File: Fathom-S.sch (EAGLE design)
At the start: 98 parts, among them IC1 LMH6643, IC2 LMH6643, IC3 ST490AB, IC4 ST490AB, IC5 FT230XS, Q1 BC817-40W, U1 MC7812, U2 MC7805, U5 MC7805, X2 USBSMD

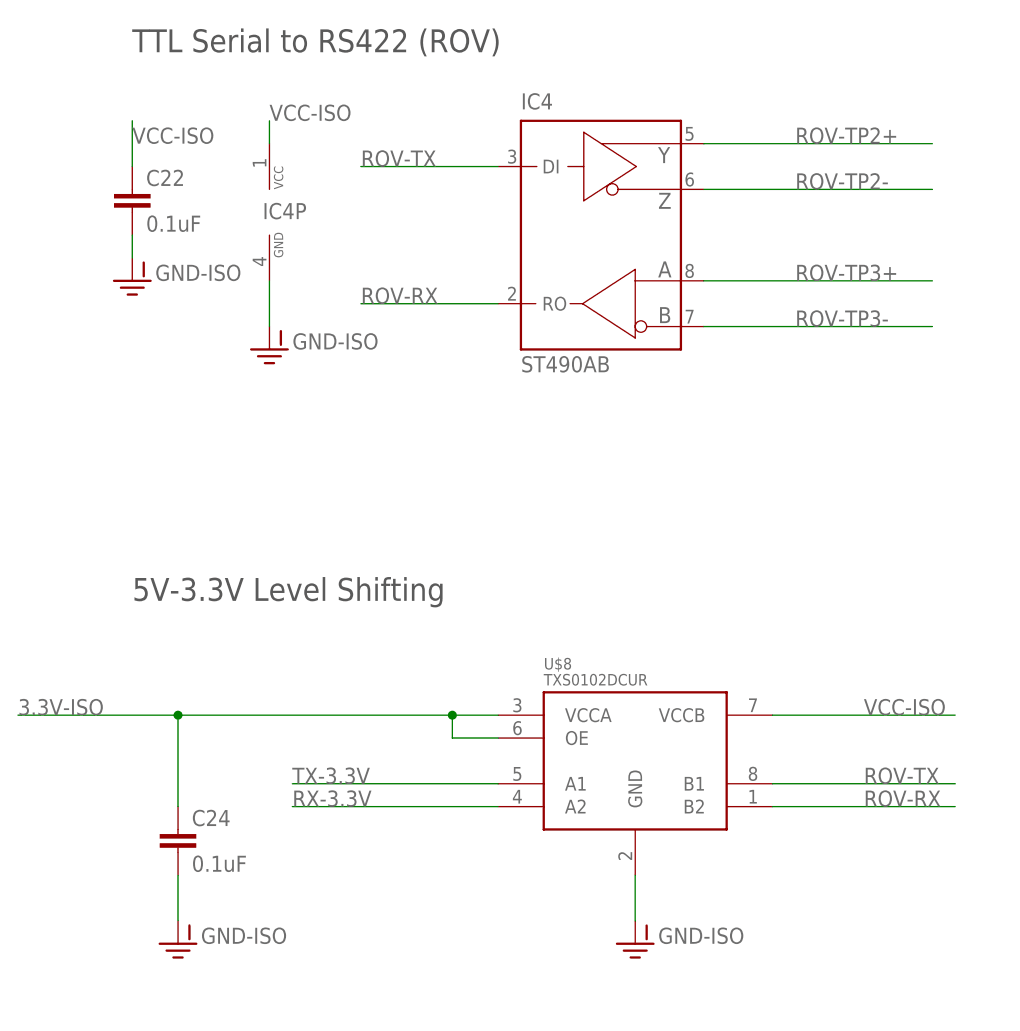
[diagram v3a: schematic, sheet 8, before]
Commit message: Switch to FET based level shifting for 5V tolerance.
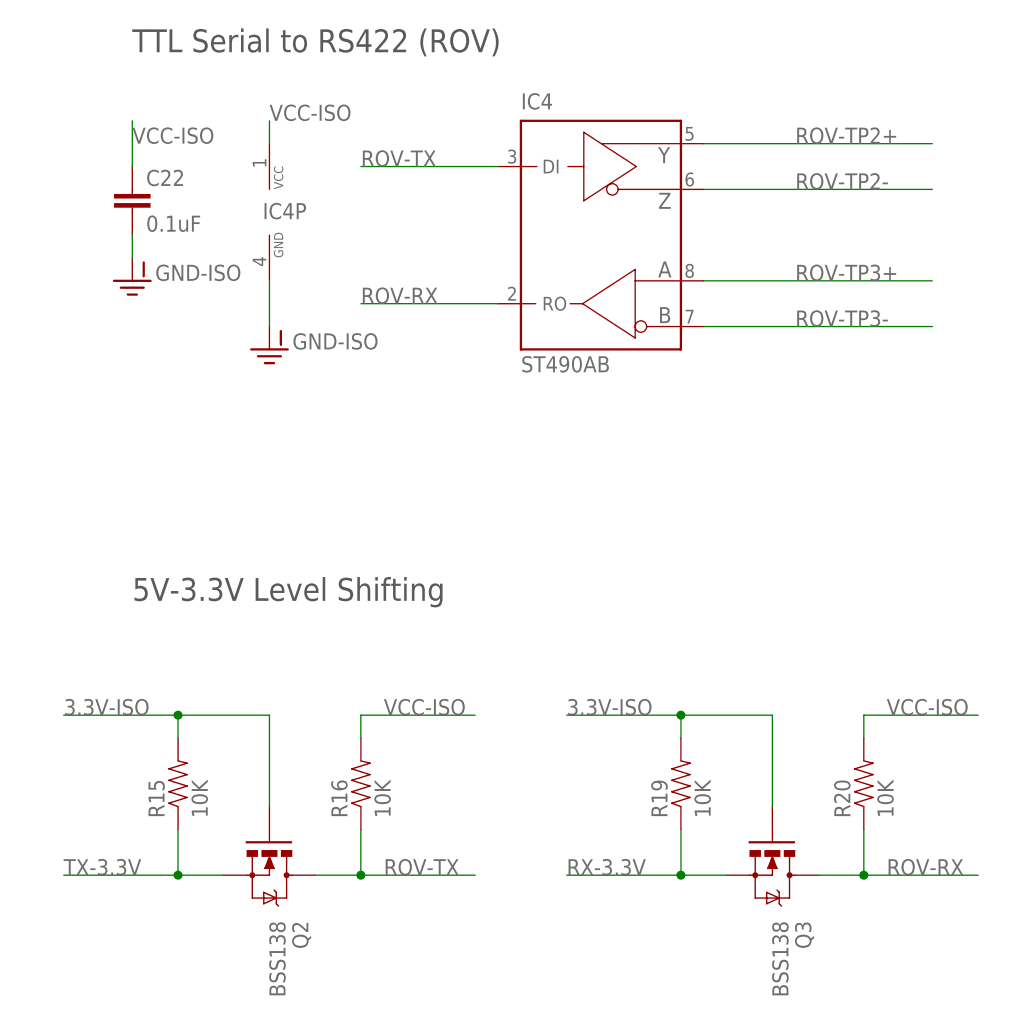
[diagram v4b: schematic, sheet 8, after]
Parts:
- removed C24: 0.1uF, SparkFun:CAP0603-CAP
- removed U$8: TXS0102DCUR, BlueRobotics-Main:TXS0102
- added Q2, Q3: BSS138, SparkFun-DiscreteSemi:MOSFET-NCHANNELBSS138
- added R15, R16, R19, R20: 10K, SparkFun:RESISTOR0603-RES
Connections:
- net 3.3V-ISO: now also Q2.G, Q3.G, R15.2, R19.2; no longer C24.1, U$8.OE, U$8.VCCA
- net GND-ISO: no longer C24.2, U$8.GND
- net ROV-RX: now also Q3.D, R20.1; no longer U$8.B2
- net ROV-TX: now also Q2.D, R16.1; no longer U$8.B1
- net RX-3.3V: now also Q3.S, R19.1; no longer U$8.A2
- net TX-3.3V: now also Q2.S, R15.1; no longer U$8.A1
- net VCC-ISO: now also R16.2, R20.2; no longer U$8.VCCB
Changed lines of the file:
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@@
 <part name="JP1" library="SparkFun-Connectors" deviceset="M04" device="PTH"/>
 <part name="FRAME8" library="BlueRobotics-Main" deviceset="FRAME-BLUEROBOTICS" device="" value="RS422 and Level Shifting"/>
-<part name="U$8" library="BlueRobotics-Main" deviceset="TXS0102" device="" value="TXS0102DCUR "/>
-<part name="GND-ISO1" library="SparkFun-Aesthetics" deviceset="GND-ISO" device=""/>
 <part name="U$15" library="BlueRobotics-Main" deviceset="VREG-MIC5365" device=""/>
 <part name="GND-ISO19" library="SparkFun-Aesthetics" deviceset="GND-ISO" device=""/>
@@
 <part name="GND-ISO20" library="SparkFun-Aesthetics" deviceset="GND-ISO" device=""/>
 <part name="GND-ISO21" library="SparkFun-Aesthetics" deviceset="GND-ISO" device=""/>
-<part name="C24" library="SparkFun" deviceset="CAP" device="0603-CAP" value="0.1uF"/>
-<part name="GND-ISO2" library="SparkFun-Aesthetics" deviceset="GND-ISO" device=""/>
 <part name="JP5" library="SparkFun-Connectors" deviceset="M02" device="PTH"/>
+<part name="Q2" library="SparkFun-DiscreteSemi" deviceset="MOSFET-NCHANNEL" device="BSS138" value="BSS138"/>
+<part name="R15" library="SparkFun" deviceset="RESISTOR" device="0603-RES" value="10K"/>
+<part name="R16" library="SparkFun" deviceset="RESISTOR" device="0603-RES" value="10K"/>
+<part name="Q3" library="SparkFun-DiscreteSemi" deviceset="MOSFET-NCHANNEL" device="BSS138" value="BSS138"/>
+<part name="R19" library="SparkFun" deviceset="RESISTOR" device="0603-RES" value="10K"/>
+<part name="R20" library="SparkFun" deviceset="RESISTOR" device="0603-RES" value="10K"/>
 </parts>
 <sheets>
@@
 <instance part="FRAME8" gate="G$1" x="0" y="0"/>
 <instance part="FRAME8" gate="G$2" x="147.32" y="0"/>
-<instance part="U$8" gate="G$1" x="127" y="73.66"/>
-<instance part="GND-ISO1" gate="G$1" x="137.16" y="60.96"/>
-<instance part="C24" gate="G$1" x="86.36" y="71.12"/>
-<instance part="GND-ISO2" gate="G$1" x="86.36" y="60.96"/>
+<instance part="Q2" gate="G$1" x="96.52" y="68.58" rot="R270"/>
+<instance part="R15" gate="G$1" x="86.36" y="78.74" rot="R90"/>
+<instance part="R16" gate="G$1" x="106.68" y="78.74" rot="R90"/>
+<instance part="Q3" gate="G$1" x="152.4" y="68.58" rot="R270"/>
+<instance part="R19" gate="G$1" x="142.24" y="78.74" rot="R90"/>
+<instance part="R20" gate="G$1" x="162.56" y="78.74" rot="R90"/>
 </instances>
 <busses>
@@
 <pinref part="GND-ISO17" gate="G$1" pin="GND-ISO"/>
 </segment>
-<segment>
-<pinref part="GND-ISO1" gate="G$1" pin="GND-ISO"/>
-<pinref part="U$8" gate="G$1" pin="GND"/>
-<wire x1="137.16" y1="63.5" x2="137.16" y2="68.58" width="0.1524" layer="91"/>
-</segment>
-<segment>
-<pinref part="GND-ISO2" gate="G$1" pin="GND-ISO"/>
-<pinref part="C24" gate="G$1" pin="2"/>
-<wire x1="86.36" y1="63.5" x2="86.36" y2="68.58" width="0.1524" layer="91"/>
-</segment>
 </net>
 <net name="VCC-ISO" class="0">
@@
 </segment>
 <segment>
-<pinref part="U$8" gate="G$1" pin="VCCB"/>
-<wire x1="152.4" y1="86.36" x2="172.72" y2="86.36" width="0.1524" layer="91"/>
-<label x="162.56" y="86.36" size="1.778" layer="95"/>
+<pinref part="R16" gate="G$1" pin="2"/>
+<wire x1="106.68" y1="83.82" x2="106.68" y2="86.36" width="0.1524" layer="91"/>
+<wire x1="106.68" y1="86.36" x2="119.38" y2="86.36" width="0.1524" layer="91"/>
+<label x="109.22" y="86.36" size="1.778" layer="95"/>
+</segment>
+<segment>
+<pinref part="R20" gate="G$1" pin="2"/>
+<wire x1="162.56" y1="83.82" x2="162.56" y2="86.36" width="0.1524" layer="91"/>
+<wire x1="162.56" y1="86.36" x2="175.26" y2="86.36" width="0.1524" layer="91"/>
+<label x="165.1" y="86.36" size="1.778" layer="95"/>
 </segment>
 </net>
@@
 </segment>
 <segment>
-<wire x1="152.4" y1="78.74" x2="172.72" y2="78.74" width="0.1524" layer="91"/>
-<pinref part="U$8" gate="G$1" pin="B1"/>
-<label x="162.56" y="78.74" size="1.778" layer="95"/>
+<pinref part="Q2" gate="G$1" pin="D"/>
+<wire x1="101.6" y1="68.58" x2="106.68" y2="68.58" width="0.1524" layer="91"/>
+<pinref part="R16" gate="G$1" pin="1"/>
+<wire x1="106.68" y1="68.58" x2="119.38" y2="68.58" width="0.1524" layer="91"/>
+<wire x1="106.68" y1="73.66" x2="106.68" y2="68.58" width="0.1524" layer="91"/>
+<junction x="106.68" y="68.58"/>
+<label x="109.22" y="68.58" size="1.778" layer="95"/>
 </segment>
 </net>
@@
 </segment>
 <segment>
-<pinref part="U$8" gate="G$1" pin="B2"/>
-<wire x1="152.4" y1="76.2" x2="172.72" y2="76.2" width="0.1524" layer="91"/>
-<label x="162.56" y="76.2" size="1.778" layer="95"/>
+<pinref part="Q3" gate="G$1" pin="D"/>
+<wire x1="157.48" y1="68.58" x2="162.56" y2="68.58" width="0.1524" layer="91"/>
+<pinref part="R20" gate="G$1" pin="1"/>
+<wire x1="162.56" y1="68.58" x2="175.26" y2="68.58" width="0.1524" layer="91"/>
+<wire x1="162.56" y1="73.66" x2="162.56" y2="68.58" width="0.1524" layer="91"/>
+<junction x="162.56" y="68.58"/>
+<label x="165.1" y="68.58" size="1.778" layer="95"/>
 </segment>
 </net>
@@
 <net name="3.3V-ISO" class="0">
 <segment>
-<pinref part="U$8" gate="G$1" pin="VCCA"/>
-<wire x1="121.92" y1="86.36" x2="116.84" y2="86.36" width="0.1524" layer="91"/>
-<label x="68.58" y="86.36" size="1.778" layer="95"/>
-<wire x1="116.84" y1="86.36" x2="86.36" y2="86.36" width="0.1524" layer="91"/>
-<pinref part="U$8" gate="G$1" pin="OE"/>
-<wire x1="86.36" y1="86.36" x2="68.58" y2="86.36" width="0.1524" layer="91"/>
-<wire x1="121.92" y1="83.82" x2="116.84" y2="83.82" width="0.1524" layer="91"/>
-<wire x1="116.84" y1="83.82" x2="116.84" y2="86.36" width="0.1524" layer="91"/>
-<junction x="116.84" y="86.36"/>
-<pinref part="C24" gate="G$1" pin="1"/>
-<wire x1="86.36" y1="76.2" x2="86.36" y2="86.36" width="0.1524" layer="91"/>
+<pinref part="R15" gate="G$1" pin="2"/>
+<wire x1="86.36" y1="83.82" x2="86.36" y2="86.36" width="0.1524" layer="91"/>
+<wire x1="86.36" y1="86.36" x2="73.66" y2="86.36" width="0.1524" layer="91"/>
+<pinref part="Q2" gate="G$1" pin="G"/>
+<wire x1="86.36" y1="86.36" x2="96.52" y2="86.36" width="0.1524" layer="91"/>
+<wire x1="96.52" y1="86.36" x2="96.52" y2="76.2" width="0.1524" layer="91"/>
 <junction x="86.36" y="86.36"/>
+<label x="73.66" y="86.36" size="1.778" layer="95"/>
+</segment>
+<segment>
+<pinref part="R19" gate="G$1" pin="2"/>
+<wire x1="142.24" y1="83.82" x2="142.24" y2="86.36" width="0.1524" layer="91"/>
+<wire x1="142.24" y1="86.36" x2="129.54" y2="86.36" width="0.1524" layer="91"/>
+<pinref part="Q3" gate="G$1" pin="G"/>
+<wire x1="142.24" y1="86.36" x2="152.4" y2="86.36" width="0.1524" layer="91"/>
+<wire x1="152.4" y1="86.36" x2="152.4" y2="76.2" width="0.1524" layer="91"/>
+<junction x="142.24" y="86.36"/>
+<label x="129.54" y="86.36" size="1.778" layer="95"/>
 </segment>
 </net>
 <net name="TX-3.3V" class="0">
 <segment>
-<pinref part="U$8" gate="G$1" pin="A1"/>
-<wire x1="121.92" y1="78.74" x2="99.06" y2="78.74" width="0.1524" layer="91"/>
-<label x="99.06" y="78.74" size="1.778" layer="95"/>
+<pinref part="Q2" gate="G$1" pin="S"/>
+<wire x1="73.66" y1="68.58" x2="86.36" y2="68.58" width="0.1524" layer="91"/>
+<pinref part="R15" gate="G$1" pin="1"/>
+<wire x1="86.36" y1="68.58" x2="91.44" y2="68.58" width="0.1524" layer="91"/>
+<wire x1="86.36" y1="68.58" x2="86.36" y2="73.66" width="0.1524" layer="91"/>
+<junction x="86.36" y="68.58"/>
+<label x="73.66" y="68.58" size="1.778" layer="95"/>
 </segment>
 </net>
 <net name="RX-3.3V" class="0">
 <segment>
-<pinref part="U$8" gate="G$1" pin="A2"/>
-<wire x1="121.92" y1="76.2" x2="99.06" y2="76.2" width="0.1524" layer="91"/>
-<label x="99.06" y="76.2" size="1.778" layer="95"/>
-</segment>
-</net>
+<pinref part="Q3" gate="G$1" pin="S"/>
+<wire x1="129.54" y1="68.58" x2="142.24" y2="68.58" width="0.1524" layer="91"/>
+<pinref part="R19" gate="G$1" pin="1"/>
+<wire x1="142.24" y1="68.58" x2="147.32" y2="68.58" width="0.1524" layer="91"/>
+<wire x1="142.24" y1="68.58" x2="142.24" y2="73.66" width="0.1524" layer="91"/>
+<junction x="142.24" y="68.58"/>
+<label x="129.54" y="68.58" size="1.778" layer="95"/>
+</segment>
+</net>

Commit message: Further updates to Rev5. First production run.
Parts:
- added TP1, TP6: -5V, BlueRobotics-Main:TEST-POINT
- added TP2: 12V, BlueRobotics-Main:TEST-POINT
- added TP3, TP5: 5V, BlueRobotics-Main:TEST-POINT
- added TP4: VIN, BlueRobotics-Main:TEST-POINT
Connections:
- net -VCC: now also TP6.TP
- net -VCC-ISO: now also TP1.TP
- net 12V-ISO: now also TP2.TP
- net ROV-VIN: now also TP4.TP
- net VCC: now also TP5.TP
- net VCC-ISO: now also TP3.TP
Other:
- note added: "Test Points"
- note removed: "Min Battery Voltage: 9V Max Battery Voltage: 26V"
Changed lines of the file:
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@@
 <part name="R19" library="SparkFun" deviceset="RESISTOR" device="0603-RES" value="10K"/>
 <part name="R20" library="SparkFun" deviceset="RESISTOR" device="0603-RES" value="10K"/>
+<part name="TP1" library="BlueRobotics-Main" deviceset="TEST-POINT" device="" value="-5V"/>
+<part name="TP2" library="BlueRobotics-Main" deviceset="TEST-POINT" device="" value="12V"/>
+<part name="TP3" library="BlueRobotics-Main" deviceset="TEST-POINT" device="" value="5V"/>
+<part name="TP4" library="BlueRobotics-Main" deviceset="TEST-POINT" device="" value="VIN"/>
+<part name="TP5" library="BlueRobotics-Main" deviceset="TEST-POINT" device="" value="5V"/>
+<part name="TP6" library="BlueRobotics-Main" deviceset="TEST-POINT" device="" value="-5V"/>
 </parts>
 <sheets>
@@
 power board)</text>
 <text x="17.78" y="106.68" size="2.54" layer="97">Switched Power Access</text>
+<text x="17.78" y="76.2" size="2.54" layer="97">Test Points</text>
 </plain>
 <instances>
@@
 <instance part="JP1" gate="G$1" x="144.78" y="139.7" rot="R180"/>
 <instance part="JP5" gate="G$1" x="17.78" y="93.98"/>
+<instance part="TP1" gate="G$1" x="17.78" y="68.58"/>
+<instance part="TP2" gate="G$1" x="17.78" y="58.42"/>
+<instance part="TP3" gate="G$1" x="17.78" y="48.26"/>
+<instance part="TP4" gate="G$1" x="17.78" y="38.1"/>
 </instances>
 <busses>
@@
 <label x="134.62" y="58.42" size="1.778" layer="95"/>
 </segment>
+<segment>
+<wire x1="17.78" y1="55.88" x2="17.78" y2="53.34" width="0.1524" layer="91"/>
+<wire x1="17.78" y1="53.34" x2="50.8" y2="53.34" width="0.1524" layer="91"/>
+<label x="38.1" y="53.34" size="1.778" layer="95"/>
+<pinref part="TP2" gate="G$1" pin="TP"/>
+</segment>
 </net>
 <net name="VCC-ISO" class="0">
@@
 <label x="106.68" y="119.38" size="1.778" layer="95"/>
 </segment>
+<segment>
+<wire x1="17.78" y1="45.72" x2="17.78" y2="43.18" width="0.1524" layer="91"/>
+<wire x1="17.78" y1="43.18" x2="50.8" y2="43.18" width="0.1524" layer="91"/>
+<label x="38.1" y="43.18" size="1.778" layer="95"/>
+<pinref part="TP3" gate="G$1" pin="TP"/>
+</segment>
 </net>
 <net name="ROV-BATT" class="0">
@@
 <wire x1="25.4" y1="96.52" x2="50.8" y2="96.52" width="0.1524" layer="91"/>
 <label x="40.64" y="96.52" size="1.778" layer="95"/>
+</segment>
+<segment>
+<wire x1="17.78" y1="35.56" x2="17.78" y2="33.02" width="0.1524" layer="91"/>
+<wire x1="17.78" y1="33.02" x2="50.8" y2="33.02" width="0.1524" layer="91"/>
+<label x="38.1" y="33.02" size="1.778" layer="95"/>
+<pinref part="TP4" gate="G$1" pin="TP"/>
+</segment>
+</net>
+<net name="-VCC-ISO" class="0">
+<segment>
+<wire x1="17.78" y1="66.04" x2="17.78" y2="63.5" width="0.1524" layer="91"/>
+<wire x1="17.78" y1="63.5" x2="50.8" y2="63.5" width="0.1524" layer="91"/>
+<label x="38.1" y="63.5" size="1.778" layer="95"/>
+<pinref part="TP1" gate="G$1" pin="TP"/>
 </segment>
 </net>
@@
 (if not using USB)
 (+7-30V)</text>
+<text x="10.16" y="71.12" size="2.54" layer="97">Test Points</text>
 </plain>
 <instances>
@@
 <instance part="JP15" gate="G$1" x="45.72" y="127" rot="R180"/>
 <instance part="U$12" gate="G$1" x="116.84" y="165.1" rot="R180"/>
+<instance part="TP5" gate="G$1" x="12.7" y="63.5"/>
+<instance part="TP6" gate="G$1" x="12.7" y="53.34"/>
 </instances>
 <busses>
@@
 <label x="10.16" y="124.46" size="1.778" layer="95"/>
 </segment>
+<segment>
+<wire x1="12.7" y1="60.96" x2="12.7" y2="58.42" width="0.1524" layer="91"/>
+<wire x1="12.7" y1="58.42" x2="45.72" y2="58.42" width="0.1524" layer="91"/>
+<label x="33.02" y="58.42" size="1.778" layer="95"/>
+<pinref part="TP5" gate="G$1" pin="TP"/>
+</segment>
 </net>
 <net name="TOP-VIN" class="0">
@@
 <wire x1="40.64" y1="152.4" x2="10.16" y2="152.4" width="0.1524" layer="91"/>
 <label x="10.16" y="152.4" size="1.778" layer="95"/>
+</segment>
+</net>
+<net name="-VCC" class="0">
+<segment>
+<wire x1="12.7" y1="50.8" x2="12.7" y2="48.26" width="0.1524" layer="91"/>
+<wire x1="12.7" y1="48.26" x2="45.72" y2="48.26" width="0.1524" layer="91"/>
+<label x="33.02" y="48.26" size="1.778" layer="95"/>
+<pinref part="TP6" gate="G$1" pin="TP"/>
 </segment>
 </net>
@@
 <text x="53.34" y="104.14" size="1.778" layer="97">ROV-ON between
 3.3V-50V</text>
-<text x="208.28" y="40.64" size="1.778" layer="97">Min Battery Voltage: 9V
-Max Battery Voltage: 26V</text>
 <text x="96.52" y="130.556" size="1.778" layer="97" rot="R90">16V</text>
 </plain>
@@
 <wire x1="144.78" y1="132.08" x2="149.86" y2="132.08" width="0.1524" layer="91"/>
 <junction x="149.86" y="132.08"/>
-<wire x1="149.86" y1="132.08" x2="180.34" y2="132.08" width="0.1524" layer="91"/>
+<wire x1="149.86" y1="132.08" x2="165.1" y2="132.08" width="0.1524" layer="91"/>
 <label x="154.94" y="132.08" size="1.778" layer="95"/>
 </segment>

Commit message: Updated files before release.
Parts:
- C13: device SparkFun-Passives:CAP_POL6032 -> BlueRobotics-Main:CAPACITOR-POLAR2413
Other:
- note added: "5V output for µC, sensors, etc. (250mA w/ 12Vin) (100mA w/ 20Vin)"
- note added: "Alternate topside power input (if not using USB) (+7-20V)"
- note added: "Battery Input (+7-20V)"
- note removed: "5V output for µC, sensors, etc. (250mA w/ 12Vin) (100mA w/ 24Vin)"
- note removed: "Alternate topside power input (if not using USB) (+7-30V)"
- note removed: "Battery Input (+9-26V)"
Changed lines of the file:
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@@
 <part name="R25" library="SparkFun-Resistors" deviceset="33KOHM1/10W1%(0603)" device="" value="10K"/>
 <part name="D1" library="SparkFun-DiscreteSemi" deviceset="DIODE-ZENER" device="3.3V" value="16V"/>
-<part name="C13" library="SparkFun-Passives" deviceset="CAP_POL" device="6032" value="33uF 20V"/>
+<part name="C13" library="BlueRobotics-Main" deviceset="CAPACITOR-POLAR" device="2413" value="33uF 20V"/>
 <part name="FRAME1" library="BlueRobotics-Main" deviceset="FRAME-BLUEROBOTICS" device="" value="Onboard Connectors &amp; Misc."/>
 <part name="FRAME2" library="BlueRobotics-Main" deviceset="FRAME-BLUEROBOTICS" device="" value="Video Amplifiers"/>
@@
 <text x="17.78" y="137.16" size="2.54" layer="97">Override ROV-on</text>
 <text x="154.94" y="167.64" size="1.778" layer="97">Battery Input
-(+9-26V)</text>
+(+7-20V)</text>
 <text x="160.02" y="134.62" size="1.778" layer="97">5V output for µC, sensors, etc.
 (250mA w/ 12Vin)
-(100mA w/ 24Vin)</text>
+(100mA w/ 20Vin)</text>
 <text x="160.02" y="55.88" size="1.778" layer="97">12V output is not guaranteed,
 so this is intended for camera with wide
@@
 <text x="129.54" y="160.02" size="1.778" layer="97">Alternate topside power input
 (if not using USB)
-(+7-30V)</text>
+(+7-20V)</text>
 <text x="10.16" y="71.12" size="2.54" layer="97">Test Points</text>
 </plain>
